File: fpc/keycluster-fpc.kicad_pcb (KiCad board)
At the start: 2 copper layers, 15 x 17 mm, 2 parts

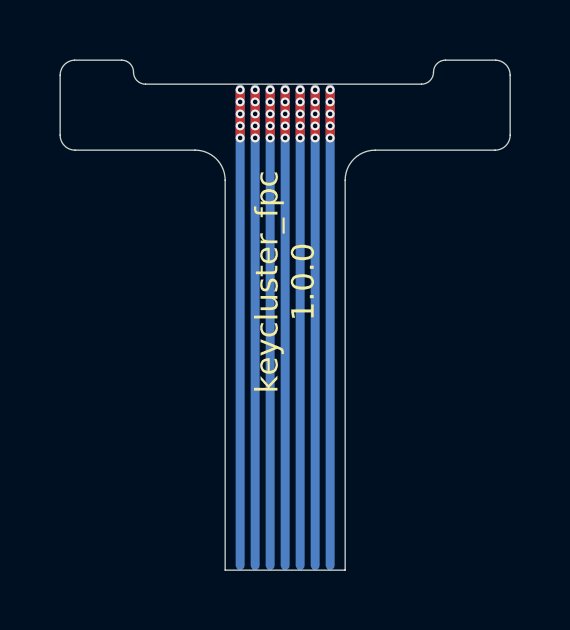
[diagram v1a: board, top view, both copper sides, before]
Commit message: Reduce FPC length by 3 mm.
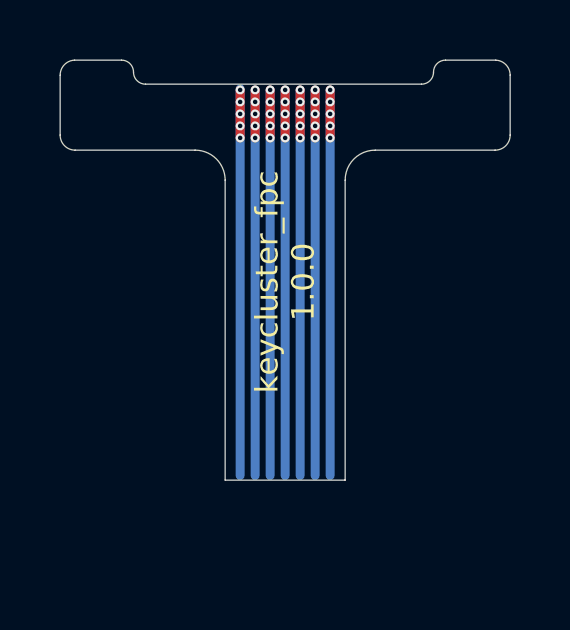
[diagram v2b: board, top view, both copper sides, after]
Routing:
- net (no net): track 122.4 -> 101.1 mm
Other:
- board size 15 x 17 mm -> 15 x 14 mm
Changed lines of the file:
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@@
     (effects (font (size 0.75 0.75) (thickness 0.15)))
   )
-  (gr_text "Stiffener TOP" (at 220.63 130.71) (layer Dwgs.User)
+  (gr_text "Stiffener TOP" (at 220.63 127.71) (layer Dwgs.User)
     (effects (font (size 1 1) (thickness 0.15)))
   )
-  (gr_text "5.00 mm" (at 220.63 123.11 90) (layer Dwgs.User)
+  (gr_text "5.00 mm" (at 220.63 120.11 90) (layer Dwgs.User)
     (effects (font (size 1 1) (thickness 0.15)))
   )
-  (gr_line (start 221.53 127.41) (end 221.63 127.41) (layer Dwgs.User) (width 0.15))
-  (gr_line (start 221.43 127.31) (end 221.73 127.31) (layer Dwgs.User) (width 0.15))
-  (gr_line (start 221.48 133.91) (end 221.68 133.91) (layer Dwgs.User) (width 0.15))
-  (gr_line (start 221.43 134.01) (end 221.68 134.01) (layer Dwgs.User) (width 0.15))
-  (gr_line (start 221.78 134.11) (end 221.38 134.11) (layer Dwgs.User) (width 0.15))
-  (gr_line (start 221.58 133.21) (end 221.78 134.11) (layer Dwgs.User) (width 0.15))
-  (gr_line (start 221.58 133.21) (end 221.38 134.11) (layer Dwgs.User) (width 0.15))
-  (gr_line (start 221.58 133.21) (end 221.58 135.76) (layer Dwgs.User) (width 0.15))
-  (gr_line (start 221.78 127.16) (end 221.38 127.16) (layer Dwgs.User) (width 0.15))
-  (gr_line (start 221.58 128.21) (end 221.78 127.16) (layer Dwgs.User) (width 0.15))
-  (gr_line (start 221.58 128.21) (end 221.38 127.16) (layer Dwgs.User) (width 0.15))
-  (gr_line (start 221.58 128.21) (end 221.58 119.51) (layer Dwgs.User) (width 0.15))
-  (gr_line (start 215.08 133.21) (end 222.58 133.21) (layer Dwgs.User) (width 0.15))
-  (gr_line (start 215.08 128.21) (end 222.58 128.21) (layer Dwgs.User) (width 0.15))
-  (gr_line (start 210.945067 130.725205) (end 214.945067 130.725205) (layer B.Mask) (width 5))
+  (gr_line (start 221.53 124.41) (end 221.63 124.41) (layer Dwgs.User) (width 0.15))
+  (gr_line (start 221.43 124.31) (end 221.73 124.31) (layer Dwgs.User) (width 0.15))
+  (gr_line (start 221.48 130.91) (end 221.68 130.91) (layer Dwgs.User) (width 0.15))
+  (gr_line (start 221.43 131.01) (end 221.68 131.01) (layer Dwgs.User) (width 0.15))
+  (gr_line (start 221.78 131.11) (end 221.38 131.11) (layer Dwgs.User) (width 0.15))
+  (gr_line (start 221.58 130.21) (end 221.78 131.11) (layer Dwgs.User) (width 0.15))
+  (gr_line (start 221.58 130.21) (end 221.38 131.11) (layer Dwgs.User) (width 0.15))
+  (gr_line (start 221.58 130.21) (end 221.58 132.76) (layer Dwgs.User) (width 0.15))
+  (gr_line (start 221.78 124.16) (end 221.38 124.16) (layer Dwgs.User) (width 0.15))
+  (gr_line (start 221.58 125.21) (end 221.78 124.16) (layer Dwgs.User) (width 0.15))
+  (gr_line (start 221.58 125.21) (end 221.38 124.16) (layer Dwgs.User) (width 0.15))
+  (gr_line (start 221.58 125.21) (end 221.58 116.51) (layer Dwgs.User) (width 0.15))
+  (gr_line (start 215.08 130.21) (end 222.58 130.21) (layer Dwgs.User) (width 0.15))
+  (gr_line (start 215.08 125.21) (end 222.58 125.21) (layer Dwgs.User) (width 0.15))
+  (gr_line (start 210.945067 127.725205) (end 214.945067 127.725205) (layer B.Mask) (width 5))
   (gr_line (start 211.35 118.008106) (end 214.65 118.008106) (layer F.Mask) (width 2))
   (gr_line (start 205.5 116.706895) (end 205.5 118.707214) (angle 90) (layer Edge.Cuts) (width 0.01))
   (gr_line (start 220.5 118.707214) (end 220.5 116.706895) (angle 90) (layer Edge.Cuts) (width 0.01))
-  (gr_line (start 211 120.207214) (end 211 133.207214) (angle 90) (layer Edge.Cuts) (width 0.01))
-  (gr_line (start 215 120.207214) (end 215 133.207214) (angle 90) (layer Edge.Cuts) (width 0.01))
+  (gr_line (start 211 120.207214) (end 211 130.207214) (angle 90) (layer Edge.Cuts) (width 0.01))
+  (gr_line (start 215 120.207214) (end 215 130.207214) (angle 90) (layer Edge.Cuts) (width 0.01))
   (gr_arc (start 205.999992 116.706885) (end 205.98 116.207214) (angle -87.71349681) (layer Edge.Cuts) (width 0.01))
   (gr_arc (start 220.000008 116.706885) (end 220.5 116.706895) (angle -87.70994515) (layer Edge.Cuts) (width 0.01))
   (gr_line (start 205.982143 116.207214) (end 207.54542 116.207214) (angle 90) (layer Edge.Cuts) (width 0.01))
   (gr_line (start 206 119.207214) (end 210 119.207214) (angle 90) (layer Edge.Cuts) (width 0.01))
-  (gr_line (start 215 133.207214) (end 211 133.207214) (angle 90) (layer Edge.Cuts) (width 0.01))
+  (gr_line (start 215 130.207214) (end 211 130.207214) (angle 90) (layer Edge.Cuts) (width 0.01))
   (gr_line (start 211 128.207214) (end 215 128.207214) (angle 90) (layer Cmts.User) (width 0.01))
   (gr_line (start 216 119.207214) (end 220 119.207214) (angle 90) (layer Edge.Cuts) (width 0.01))
@@
   (gr_arc (start 210.000001 120.207211) (end 211 120.207214) (angle -90.00215464) (layer Edge.Cuts) (width 0.01))
   (gr_arc (start 215.999999 120.207211) (end 216 119.207214) (angle -89.99952954) (layer Edge.Cuts) (width 0.01))
-  (segment (start 212.5 133.05) (end 212.5 117.162224) (width 0.3) (layer B.Cu) (net 0))
-  (segment (start 213 133.05) (end 213 117.162224) (width 0.3) (layer B.Cu) (net 0))
-  (segment (start 213.5 133.05) (end 213.5 117.162224) (width 0.3) (layer B.Cu) (net 0))
-  (segment (start 214 133.05) (end 214 117.162224) (width 0.3) (layer B.Cu) (net 0))
-  (segment (start 214.5 133.05) (end 214.5 117.162224) (width 0.3) (layer B.Cu) (net 0))
-  (segment (start 212 133.05) (end 212 117.162224) (width 0.3) (layer B.Cu) (net 0))
-  (segment (start 211.5 133.05) (end 211.5 117.5) (width 0.3) (layer B.Cu) (net 0))
   (via (at 211.5 117.2) (size 0.3) (drill 0.15) (layers F.Cu B.Cu) (net 0))
   (segment (start 211.5 117.5) (end 211.5 117.162224) (width 0.3) (layer B.Cu) (net 0))
@@
   (segment (start 214 117.2) (end 214 118.8) (width 0.3) (layer F.Cu) (net 0))
   (segment (start 214.5 117.2) (end 214.5 118.8) (width 0.3) (layer F.Cu) (net 0))
+  (segment (start 211.5 117.6) (end 211.5 130.052204) (width 0.3) (layer B.Cu) (net 0))
+  (segment (start 212 117.2) (end 212 130.052204) (width 0.3) (layer B.Cu) (net 0))
+  (segment (start 212.5 117.2) (end 212.5 130.052204) (width 0.3) (layer B.Cu) (net 0))
+  (segment (start 213 117.2) (end 213 130.052204) (width 0.3) (layer B.Cu) (net 0))
+  (segment (start 213.5 117.2) (end 213.5 130.052204) (width 0.3) (layer B.Cu) (net 0))
+  (segment (start 214 117.2) (end 214 130.052204) (width 0.3) (layer B.Cu) (net 0))
+  (segment (start 214.5 117.2) (end 214.5 130.052204) (width 0.3) (layer B.Cu) (net 0))
 )

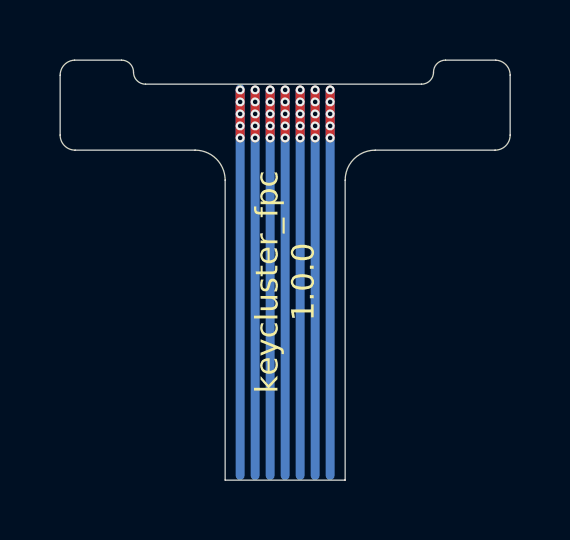
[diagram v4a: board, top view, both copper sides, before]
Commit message: Increase key cluster silk screen text and shorten it to be manufacturable.
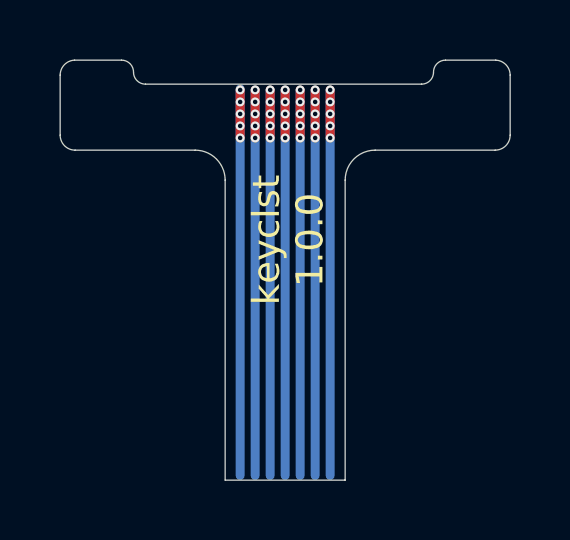
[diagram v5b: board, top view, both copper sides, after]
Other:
- board text added: "keyclst 1.0.0"
- board text removed: "keycluster_fpc 1.0.0"
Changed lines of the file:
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@@
   )
   (gr_line (start 206 117.695524) (end 220 117.695524) (layer B.Mask) (width 3))
-  (gr_text "keycluster_fpc\n1.0.0" (at 213 123.6 90) (layer F.SilkS)
-    (effects (font (size 0.75 0.75) (thickness 0.15)))
+  (gr_text "keyclst\n1.0.0" (at 213.1 122.2 90) (layer F.SilkS)
+    (effects (font (size 0.9 0.9) (thickness 0.17)))
   )
   (gr_text "Stiffener TOP" (at 222.63 127.71) (layer Dwgs.User)

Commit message: Bump FPC version to 1.1.0
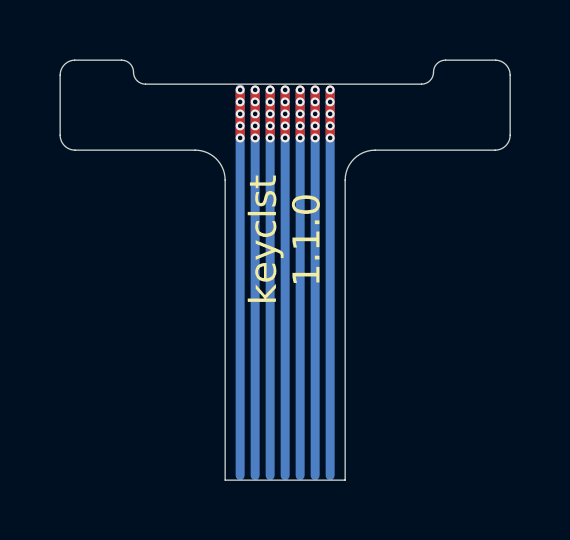
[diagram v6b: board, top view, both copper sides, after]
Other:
- board text added: "keyclst 1.1.0"
- board text removed: "keyclst 1.0.0"
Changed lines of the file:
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@@
   (title_block
     (title "UHK Key cluster FPC")
-    (rev 1.0.0)
+    (rev 1.1.0)
     (company "Ultimate Gadget Laboratories Kft.")
   )
@@
   )
   (gr_line (start 206 117.695524) (end 220 117.695524) (layer B.Mask) (width 3))
-  (gr_text "keyclst\n1.0.0" (at 213.1 122.2 90) (layer F.SilkS)
+  (gr_text "keyclst\n1.1.0" (at 213 122.2 90) (layer F.SilkS)
     (effects (font (size 0.9 0.9) (thickness 0.17)))
   )

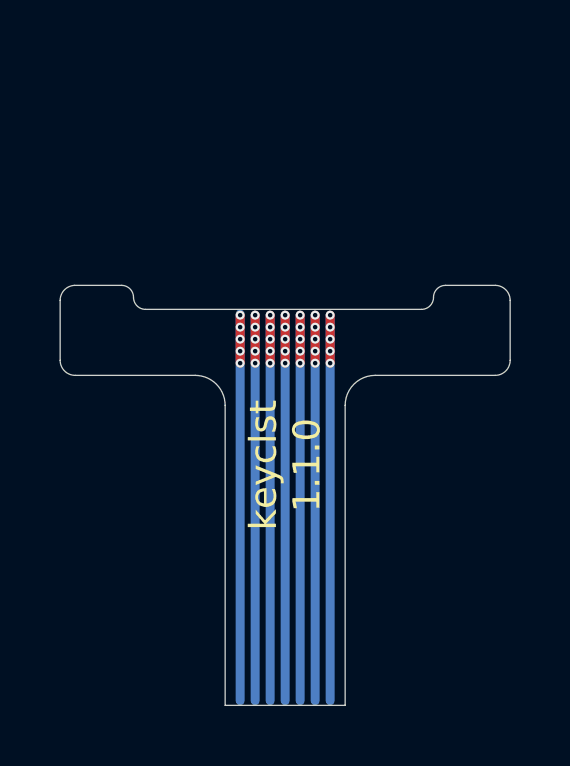
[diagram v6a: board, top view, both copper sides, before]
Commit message: Update FPC contour.
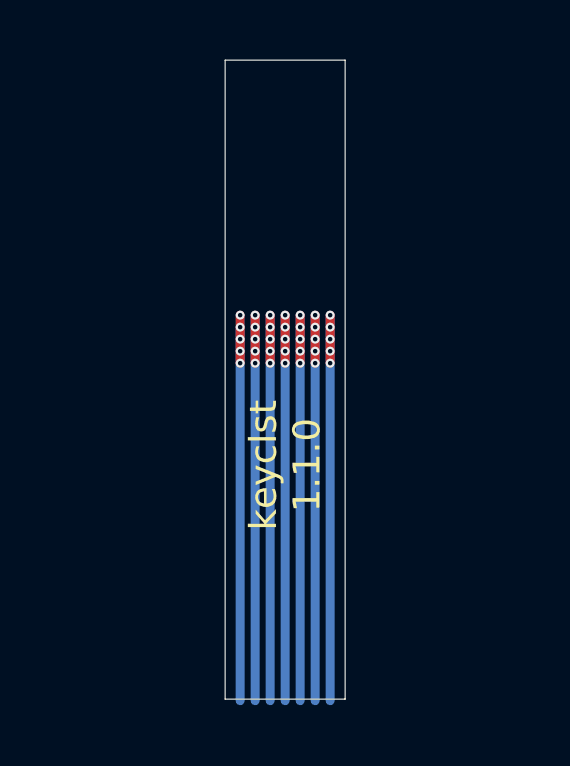
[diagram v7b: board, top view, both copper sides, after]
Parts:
- removed ? (x2): , UGL:hole_1.2000000476837158mm
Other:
- board size 15 x 14 mm -> 4 x 21.3 mm
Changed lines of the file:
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@@
-(kicad_pcb (version 20171130) (host pcbnew 5.1.6-c6e7f7d~86~ubuntu18.04.1)
+(kicad_pcb (version 20171130) (host pcbnew 5.1.6-c6e7f7d~87~ubuntu20.04.1)
   (general
     (thickness 1.6)
-    (drawings 43)
-    (tracks 50)
+    (drawings 22)
+    (tracks 49)
     (zones 0)
-    (modules 2)
+    (modules 0)
     (nets 1)
   )
@@
     (diff_pair_gap 0.25)
   )
-  (module UGL:hole_1.2000000476837158mm (layer F.Cu)
-    (at 219.222717 117.76)
-    (attr virtual)
-    (fp_text reference "" (at 0 0) (layer F.SilkS)
-      (effects (font (size 1.27 1.27) (thickness 0.15)))
-    )
-    (fp_text value "" (at 0 0) (layer F.SilkS)
-      (effects (font (size 1.27 1.27) (thickness 0.15)))
-    )
-    (pad "" np_thru_hole oval (at 0 0) (size 1.5 1.89) (drill oval 1.5 1.89) (layers *.Cu *.Mask)
-      (clearance 0.00001))
-  )
-  (module UGL:hole_1.2000000476837158mm (layer F.Cu)
-    (at 206.72271 117.76)
-    (attr virtual)
-    (fp_text reference "" (at 0 0) (layer F.SilkS)
-      (effects (font (size 1.27 1.27) (thickness 0.15)))
-    )
-    (fp_text value "" (at 0 0) (layer F.SilkS)
-      (effects (font (size 1.27 1.27) (thickness 0.15)))
-    )
-    (pad "" np_thru_hole oval (at 0 0) (size 1.5 1.89) (drill oval 1.5 1.89) (layers *.Cu *.Mask)
-      (clearance 0.00001))
-  )
-  (gr_line (start 206 117.695524) (end 220 117.695524) (layer B.Mask) (width 3))
   (gr_text "keyclst\n1.1.0" (at 213 122.2 90) (layer F.SilkS)
     (effects (font (size 0.9 0.9) (thickness 0.17)))
   )
-  (gr_text "Stiffener TOP" (at 222.63 127.71) (layer Dwgs.User)
+  (gr_text "Stiffener TOP" (at 222.63 127.51) (layer Dwgs.User)
     (effects (font (size 1 1) (thickness 0.15)))
   )
-  (gr_text "5.00 mm" (at 222.63 120.11 90) (layer Dwgs.User)
+  (gr_text "5.00 mm" (at 222.63 119.91 90) (layer Dwgs.User)
     (effects (font (size 1 1) (thickness 0.15)))
   )
-  (gr_line (start 223.53 124.41) (end 223.63 124.41) (layer Dwgs.User) (width 0.15))
-  (gr_line (start 223.43 124.31) (end 223.73 124.31) (layer Dwgs.User) (width 0.15))
-  (gr_line (start 223.48 130.91) (end 223.68 130.91) (layer Dwgs.User) (width 0.15))
-  (gr_line (start 223.43 131.01) (end 223.68 131.01) (layer Dwgs.User) (width 0.15))
-  (gr_line (start 223.78 131.11) (end 223.38 131.11) (layer Dwgs.User) (width 0.15))
-  (gr_line (start 223.58 130.21) (end 223.78 131.11) (layer Dwgs.User) (width 0.15))
-  (gr_line (start 223.58 130.21) (end 223.38 131.11) (layer Dwgs.User) (width 0.15))
-  (gr_line (start 223.58 130.21) (end 223.58 132.76) (layer Dwgs.User) (width 0.15))
-  (gr_line (start 223.78 124.16) (end 223.38 124.16) (layer Dwgs.User) (width 0.15))
-  (gr_line (start 223.58 125.21) (end 223.78 124.16) (layer Dwgs.User) (width 0.15))
-  (gr_line (start 223.58 125.21) (end 223.38 124.16) (layer Dwgs.User) (width 0.15))
-  (gr_line (start 223.58 125.21) (end 223.58 116.51) (layer Dwgs.User) (width 0.15))
-  (gr_line (start 215 130.21) (end 224.58 130.21) (layer Dwgs.User) (width 0.15))
-  (gr_line (start 215 125.21) (end 224.58 125.21) (layer Dwgs.User) (width 0.15))
-  (gr_line (start 210.945067 127.725205) (end 214.945067 127.725205) (layer B.Mask) (width 5))
-  (gr_line (start 211.35 118.008106) (end 214.65 118.008106) (layer F.Mask) (width 2))
-  (gr_line (start 205.5 116.706895) (end 205.5 118.707214) (angle 90) (layer Edge.Cuts) (width 0.01))
-  (gr_line (start 220.5 118.707214) (end 220.5 116.706895) (angle 90) (layer Edge.Cuts) (width 0.01))
-  (gr_line (start 211 120.207214) (end 211 130.207214) (angle 90) (layer Edge.Cuts) (width 0.01))
-  (gr_line (start 215 120.207214) (end 215 130.207214) (angle 90) (layer Edge.Cuts) (width 0.01))
-  (gr_arc (start 205.999992 116.706885) (end 205.98 116.207214) (angle -87.71349681) (layer Edge.Cuts) (width 0.01))
-  (gr_arc (start 220.000008 116.706885) (end 220.5 116.706895) (angle -87.70994515) (layer Edge.Cuts) (width 0.01))
-  (gr_line (start 205.982143 116.207214) (end 207.54542 116.207214) (angle 90) (layer Edge.Cuts) (width 0.01))
-  (gr_line (start 206 119.207214) (end 210 119.207214) (angle 90) (layer Edge.Cuts) (width 0.01))
-  (gr_line (start 215 130.207214) (end 211 130.207214) (angle 90) (layer Edge.Cuts) (width 0.01))
-  (gr_line (start 211 125.207214) (end 215 125.207214) (angle 90) (layer Cmts.User) (width 0.01))
-  (gr_line (start 216 119.207214) (end 220 119.207214) (angle 90) (layer Edge.Cuts) (width 0.01))
-  (gr_line (start 217.54542 117.007214) (end 208.34542 117.007214) (angle 90) (layer Edge.Cuts) (width 0.01))
-  (gr_arc (start 205.999992 118.707219) (end 205.5 118.707214) (angle -90.0025559) (layer Edge.Cuts) (width 0.01))
-  (gr_arc (start 220.000008 118.707219) (end 220 119.207214) (angle -90.00780572) (layer Edge.Cuts) (width 0.01))
-  (gr_line (start 217.94542 116.607214) (end 217.94542 116.607214) (angle 90) (layer Edge.Cuts) (width 0.01))
-  (gr_line (start 207.94542 116.607214) (end 207.94542 116.607214) (angle 90) (layer Edge.Cuts) (width 0.01))
-  (gr_line (start 218.34542 116.207214) (end 220.017857 116.207214) (angle 90) (layer Edge.Cuts) (width 0.01))
-  (gr_arc (start 217.54542 116.607215) (end 217.54542 117.007214) (angle -89.99932997) (layer Edge.Cuts) (width 0.01))
-  (gr_arc (start 218.345434 116.607226) (end 218.34542 116.207214) (angle -89.98423066) (layer Edge.Cuts) (width 0.01))
-  (gr_arc (start 208.345427 116.607215) (end 207.94542 116.607214) (angle -90.00570683) (layer Edge.Cuts) (width 0.01))
-  (gr_arc (start 207.54542 116.607226) (end 207.94542 116.607214) (angle -89.97978138) (layer Edge.Cuts) (width 0.01))
-  (gr_arc (start 210.000001 120.207211) (end 211 120.207214) (angle -90.00215464) (layer Edge.Cuts) (width 0.01))
-  (gr_arc (start 215.999999 120.207211) (end 216 119.207214) (angle -89.99952954) (layer Edge.Cuts) (width 0.01))
+  (gr_line (start 223.53 124.21) (end 223.63 124.21) (layer Dwgs.User) (width 0.15))
+  (gr_line (start 223.43 124.11) (end 223.73 124.11) (layer Dwgs.User) (width 0.15))
+  (gr_line (start 223.48 130.71) (end 223.68 130.71) (layer Dwgs.User) (width 0.15))
+  (gr_line (start 223.43 130.81) (end 223.68 130.81) (layer Dwgs.User) (width 0.15))
+  (gr_line (start 223.78 130.91) (end 223.38 130.91) (layer Dwgs.User) (width 0.15))
+  (gr_line (start 223.58 130.01) (end 223.78 130.91) (layer Dwgs.User) (width 0.15))
+  (gr_line (start 223.58 130.01) (end 223.38 130.91) (layer Dwgs.User) (width 0.15))
+  (gr_line (start 223.58 130.01) (end 223.58 132.56) (layer Dwgs.User) (width 0.15))
+  (gr_line (start 223.78 123.96) (end 223.38 123.96) (layer Dwgs.User) (width 0.15))
+  (gr_line (start 223.58 125.01) (end 223.78 123.96) (layer Dwgs.User) (width 0.15))
+  (gr_line (start 223.58 125.01) (end 223.38 123.96) (layer Dwgs.User) (width 0.15))
+  (gr_line (start 223.58 125.01) (end 223.58 116.31) (layer Dwgs.User) (width 0.15))
+  (gr_line (start 215 130.01) (end 224.58 130.01) (layer Dwgs.User) (width 0.15))
+  (gr_line (start 215 125.01) (end 224.58 125.01) (layer Dwgs.User) (width 0.15))
+  (gr_line (start 211 108.7) (end 211 130) (angle 90) (layer Edge.Cuts) (width 0.01))
+  (gr_line (start 215 108.7) (end 215 130) (angle 90) (layer Edge.Cuts) (width 0.01))
+  (gr_line (start 215 130) (end 211 130) (angle 90) (layer Edge.Cuts) (width 0.01))
+  (gr_line (start 211 125.00384) (end 215 125.00384) (angle 90) (layer Cmts.User) (width 0.01))
+  (gr_line (start 215 108.7) (end 211 108.7) (angle 90) (layer Edge.Cuts) (width 0.01))
   (via (at 211.5 117.2) (size 0.3) (drill 0.15) (layers F.Cu B.Cu) (net 0))
-  (segment (start 211.5 117.5) (end 211.5 117.162224) (width 0.3) (layer B.Cu) (net 0))
   (via (at 212 117.2) (size 0.3) (drill 0.15) (layers F.Cu B.Cu) (net 0))
   (via (at 212.5 117.2) (size 0.3) (drill 0.15) (layers F.Cu B.Cu) (net 0))

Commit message: Add FPC tracks and bump version to 2.0.0
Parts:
- added REF**: Keycluster_FPC_7x0.5_pads, UGL:Keycluster_FPC_7x0.5_pads, F.Cu at (213.0, 110.0)
- added REF**: Keycluster_FPC_7x0.5_pads, UGL:Keycluster_FPC_7x0.5_pads, F.Cu at (213.0, 128.8)
- added REF**: Keycluster_FPC_7x0.5_pads, UGL:Keycluster_FPC_7x0.5_pads, B.Cu at (213.0, 110.0)
- added REF**: Keycluster_FPC_7x0.5_pads, UGL:Keycluster_FPC_7x0.5_pads, F.Cu at (213.0, 1010.0)
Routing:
- net (no net): track 100.8 -> 132.6 mm, vias 35 -> 49
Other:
- board text added: "Stiffener BOTTOM"
- board text added: "keycluster_fpc 2.0.0"
- board text removed: "Stiffener TOP"
- board text removed: "keyclst 1.1.0"
